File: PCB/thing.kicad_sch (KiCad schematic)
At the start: 6 parts, among them U1 Seeed Studio XIAO SAMD21

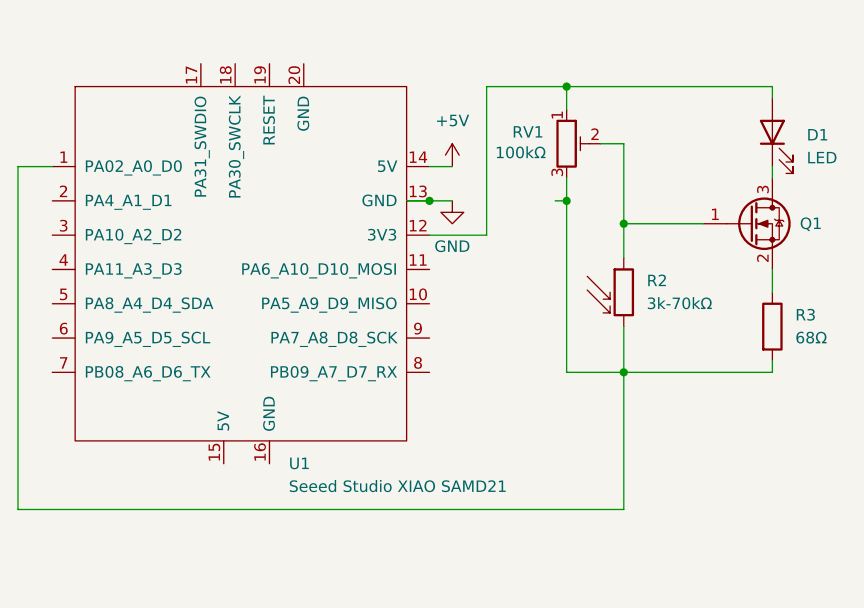
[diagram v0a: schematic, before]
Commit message: Tie all xiao gnd outs to ground
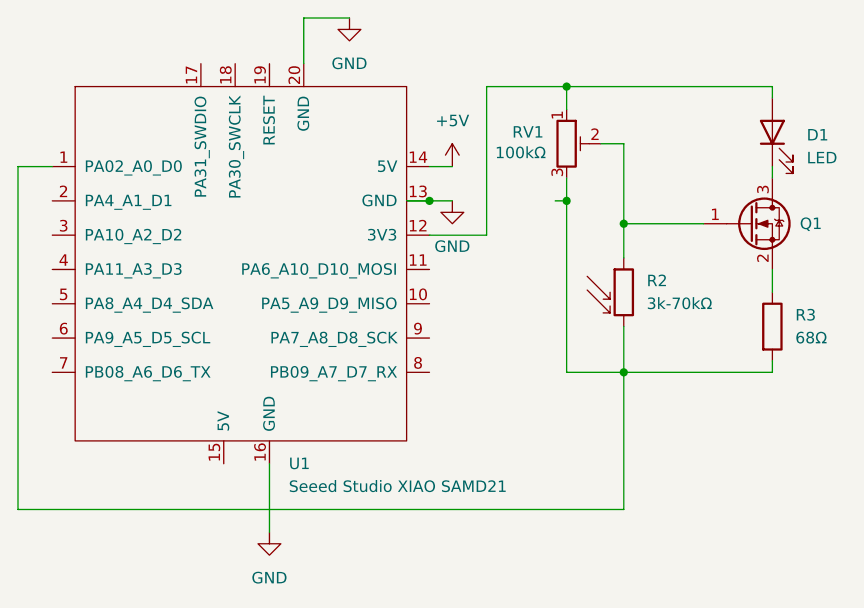
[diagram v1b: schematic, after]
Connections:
- net GND: now also U1.16 (GND), U1.20 (GND)
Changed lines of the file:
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@@
+	(wire
+		(pts
+			(xy 138.43 36.83) (xy 143.51 36.83)
+		)
+		(stroke
+			(width 0)
+			(type default)
+		)
+	)
 	(wire
 		(pts
@@
 	(wire
 		(pts
+			(xy 138.43 41.91) (xy 138.43 36.83)
+		)
+		(stroke
+			(width 0)
+			(type default)
+		)
+	)
+	(wire
+		(pts
 			(xy 158.75 44.45) (xy 167.64 44.45)
 		)
@@
 		(pts
 			(xy 152.4 57.15) (xy 149.86 57.15)
+		)
+		(stroke
+			(width 0)
+			(type default)
+		)
+	)
+	(wire
+		(pts
+			(xy 134.62 86.36) (xy 134.62 93.98)
 		)
 		(stroke
@@
 	)
 	(symbol
+		(lib_id "power:GND")
+		(at 134.62 93.98 0)
+		(unit 1)
+		(exclude_from_sim no)
+		(in_bom yes)
+		(on_board yes)
+		(dnp no)
+		(fields_autoplaced yes)
+		(property "Reference" "#PWR03"
+			(at 134.62 100.33 0)
+			(effects
+				(font
+					(size 1.27 1.27)
+				)
+				(hide yes)
+			)
+		)
+		(property "Value" "GND"
+			(at 134.62 99.06 0)
+			(effects
+				(font
+					(size 1.27 1.27)
+				)
+			)
+		)
+		(property "Footprint" ""
+			(at 134.62 93.98 0)
+			(effects
+				(font
+					(size 1.27 1.27)
+				)
+				(hide yes)
+			)
+		)
+		(property "Datasheet" ""
+			(at 134.62 93.98 0)
+			(effects
+				(font
+					(size 1.27 1.27)
+				)
+				(hide yes)
+			)
+		)
+		(property "Description" "Power symbol creates a global label with name \"GND\" , ground"
+			(at 134.62 93.98 0)
+			(effects
+				(font
+					(size 1.27 1.27)
+				)
+				(hide yes)
+			)
+		)
+		(pin "1"
+		)
+		(instances
+			(project "thing"
+				(path "/54a3e53b-4573-43bc-9261-ecb3a85bc71e"
+					(reference "#PWR03")
+					(unit 1)
+				)
+			)
+		)
+	)
+	(symbol
 		(lib_id "Seeed_Studio_XIAO_Series:Seeed Studio XIAO SAMD21")
 		(at 132.08 64.77 0)
@@
 					(unit 1)
 				)
+			)
+		)
+	)
+	(symbol
+		(lib_id "power:GND")
+		(at 143.51 36.83 0)
+		(unit 1)
+		(exclude_from_sim no)
+		(in_bom yes)
+		(on_board yes)
+		(dnp no)
+		(fields_autoplaced yes)
+		(property "Reference" "#PWR04"
+			(at 143.51 43.18 0)
+			(effects
+				(font
+					(size 1.27 1.27)
+				)
+				(hide yes)
+			)
+		)
+		(property "Value" "GND"
+			(at 143.51 41.91 0)
+			(effects
+				(font
+					(size 1.27 1.27)
+				)
+			)
+		)
+		(property "Footprint" ""
+			(at 143.51 36.83 0)
+			(effects
+				(font
+					(size 1.27 1.27)
+				)
+				(hide yes)
+			)
+		)
+		(property "Datasheet" ""
+			(at 143.51 36.83 0)
+			(effects
+				(font
+					(size 1.27 1.27)
+				)
+				(hide yes)
+			)
+		)
+		(property "Description" "Power symbol creates a global label with name \"GND\" , ground"
+			(at 143.51 36.83 0)
+			(effects
+				(font
+					(size 1.27 1.27)
+				)
+				(hide yes)
+			)
+		)
+		(pin "1"
+		)
+		(instances
+			(project "thing"
+				(path "/54a3e53b-4573-43bc-9261-ecb3a85bc71e"
+					(reference "#PWR04")
+					(unit 1)
+				)
